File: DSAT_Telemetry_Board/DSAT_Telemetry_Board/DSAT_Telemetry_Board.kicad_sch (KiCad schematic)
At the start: 24 parts

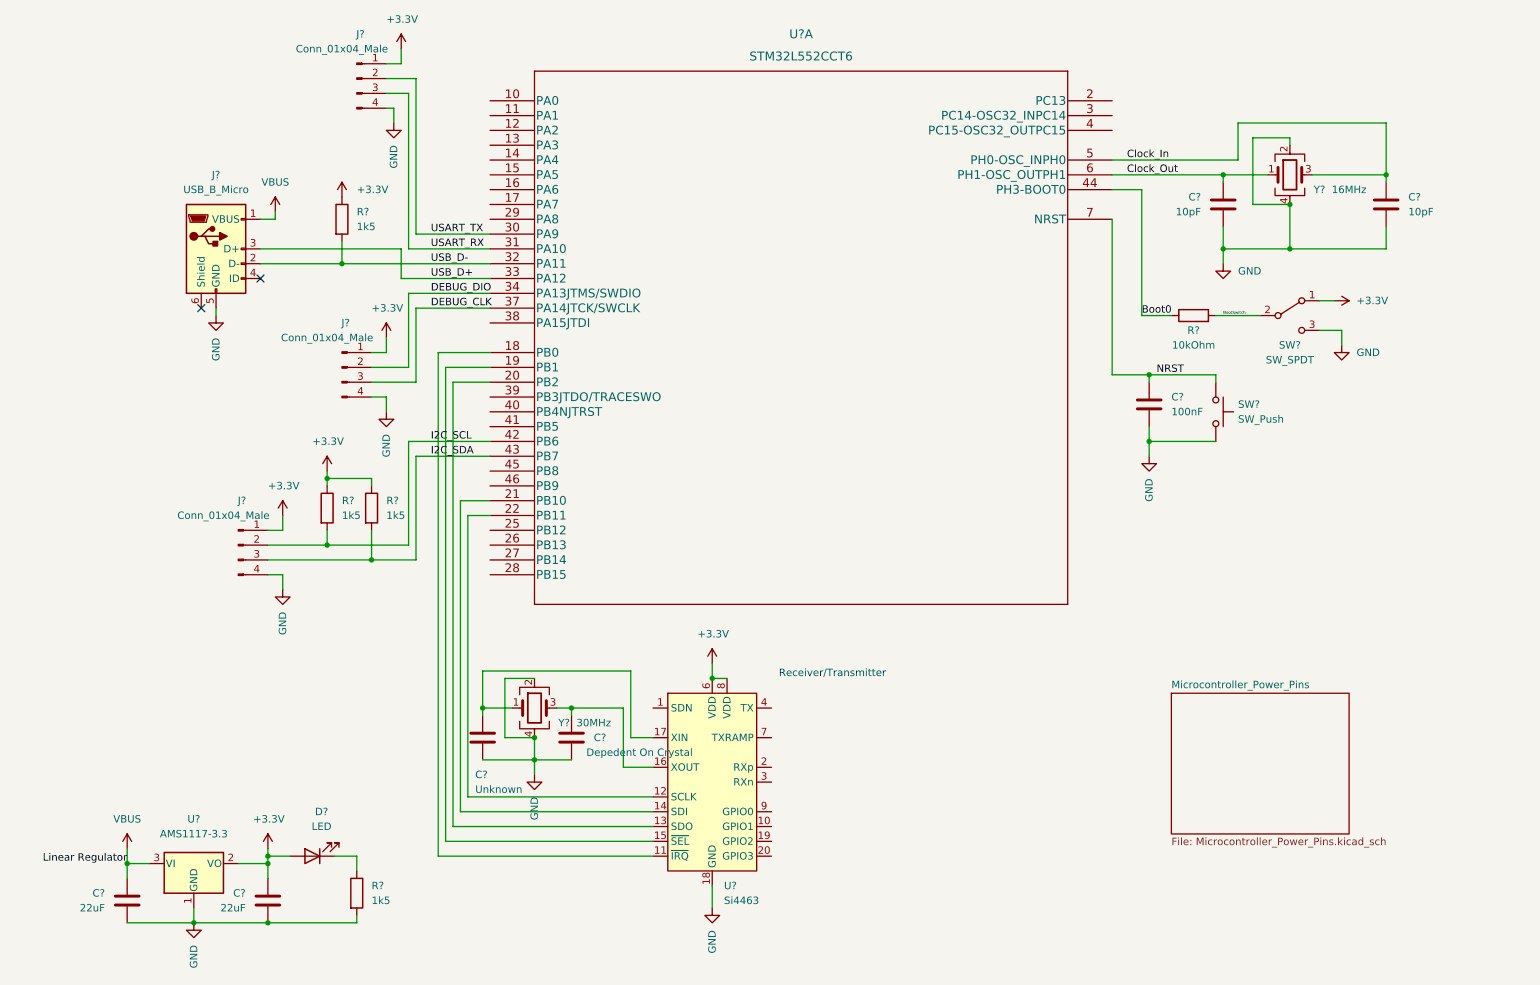
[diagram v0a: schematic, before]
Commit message: Added Hiarchical Sheets
Placed Modules into hiarchical sheets
Added Power supply section + Transcievers
Need to finish conncecting SI transciever chips and the bias tee on the chips + duplexer + LNA
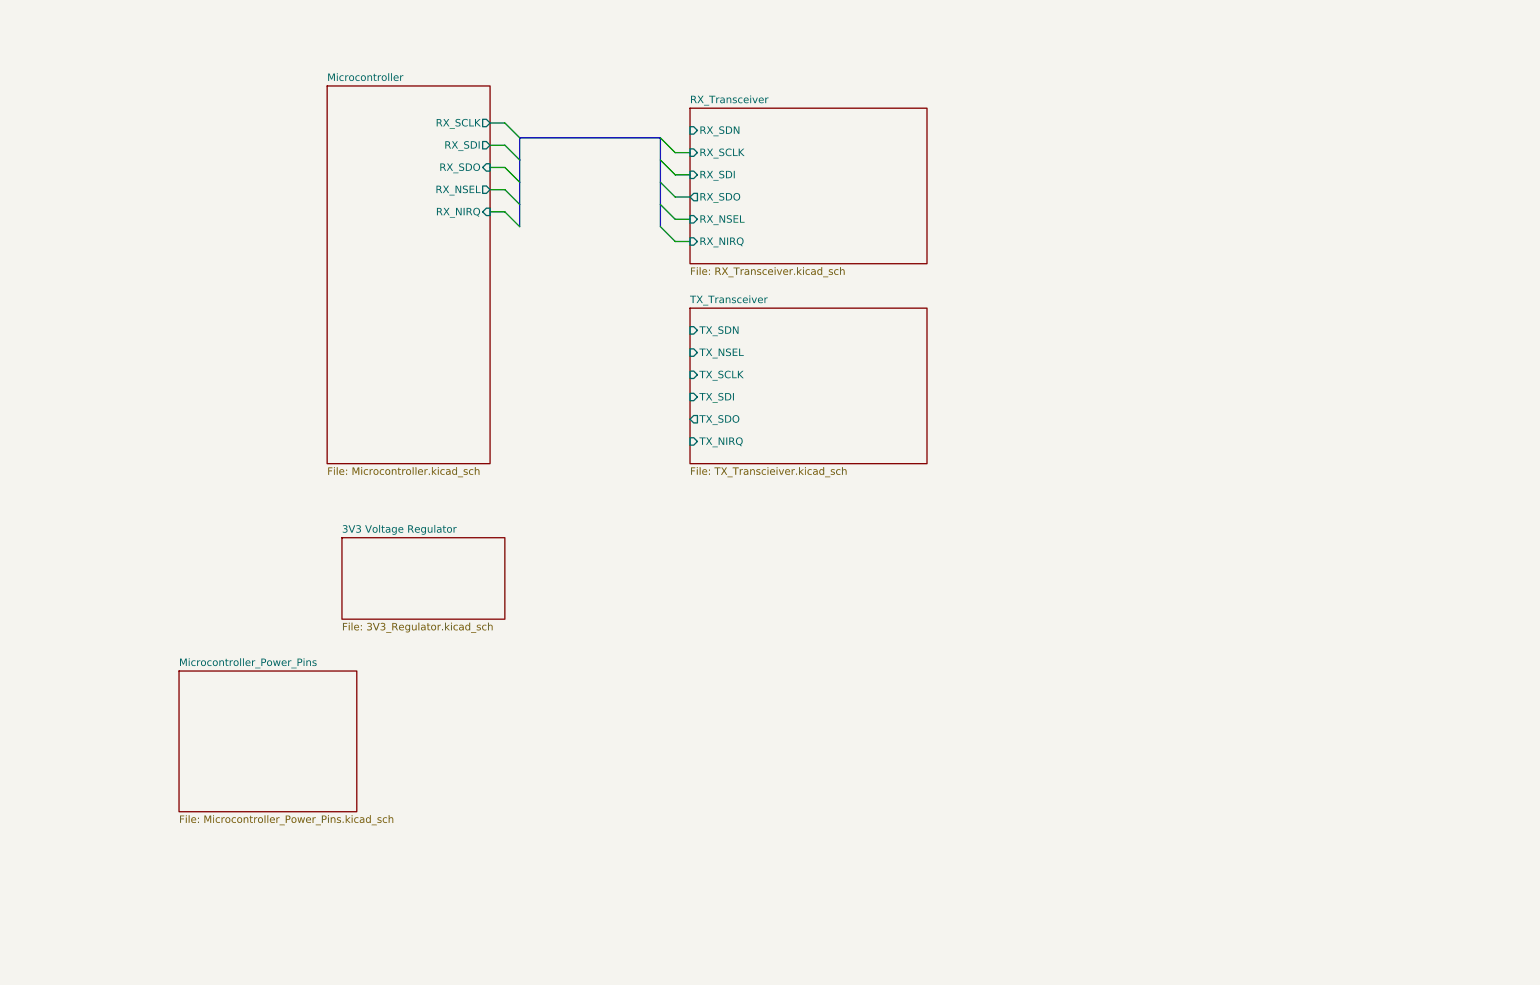
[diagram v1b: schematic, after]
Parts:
- removed C?: Unknown, symbol Device:C
- removed C? (x2): 22uF, symbol Device:C
- removed C?: Depedent On Crystal, symbol Device:C
- removed C?: 100nF, symbol Device:C
- removed C? (x2): 10pF, symbol Device:C
- removed D?: LED, symbol Device:LED
- removed J?: USB_B_Micro, symbol Connector:USB_B_Micro
- removed J? (x3): Conn_01x04_Male, symbol Connector:Conn_01x04_Male
- removed R? (x4): 1k5, symbol Device:R
- removed R?: 10kOhm, symbol Device:R
- removed SW?: SW_SPDT, symbol Switch:SW_SPDT
- removed SW?: SW_Push, symbol Switch:SW_Push
- removed U?: Si4463, Package_DFN_QFN:QFN-20-1EP_4x4mm_P0.5mm_EP2.6x2.6mm_ThermalVias, symbol RF:Si4463
- removed U?: AMS1117-3.3, Package_TO_SOT_SMD:SOT-223-3_TabPin2, symbol Regulator_Linear:AMS1117-3.3
- removed U?: STM32L552CCT6, LQFP-48, symbol STM32L5:STM32L552CCT6
- removed Y?: 16MHz, symbol Device:Crystal_GND24
- removed Y?: 30MHz, symbol Device:Crystal_GND24
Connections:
- no-connect marks 2 -> 0
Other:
- added sheet 3V3 Voltage Regulator (3V3_Regulator.kicad_sch)
- added sheet Microcontroller (Microcontroller.kicad_sch)
- added sheet RX_Transceiver (RX_Transceiver.kicad_sch)
- added sheet TX_Transceiver (TX_Transcieiver.kicad_sch)
- note removed: "Receiver/Transmitter"

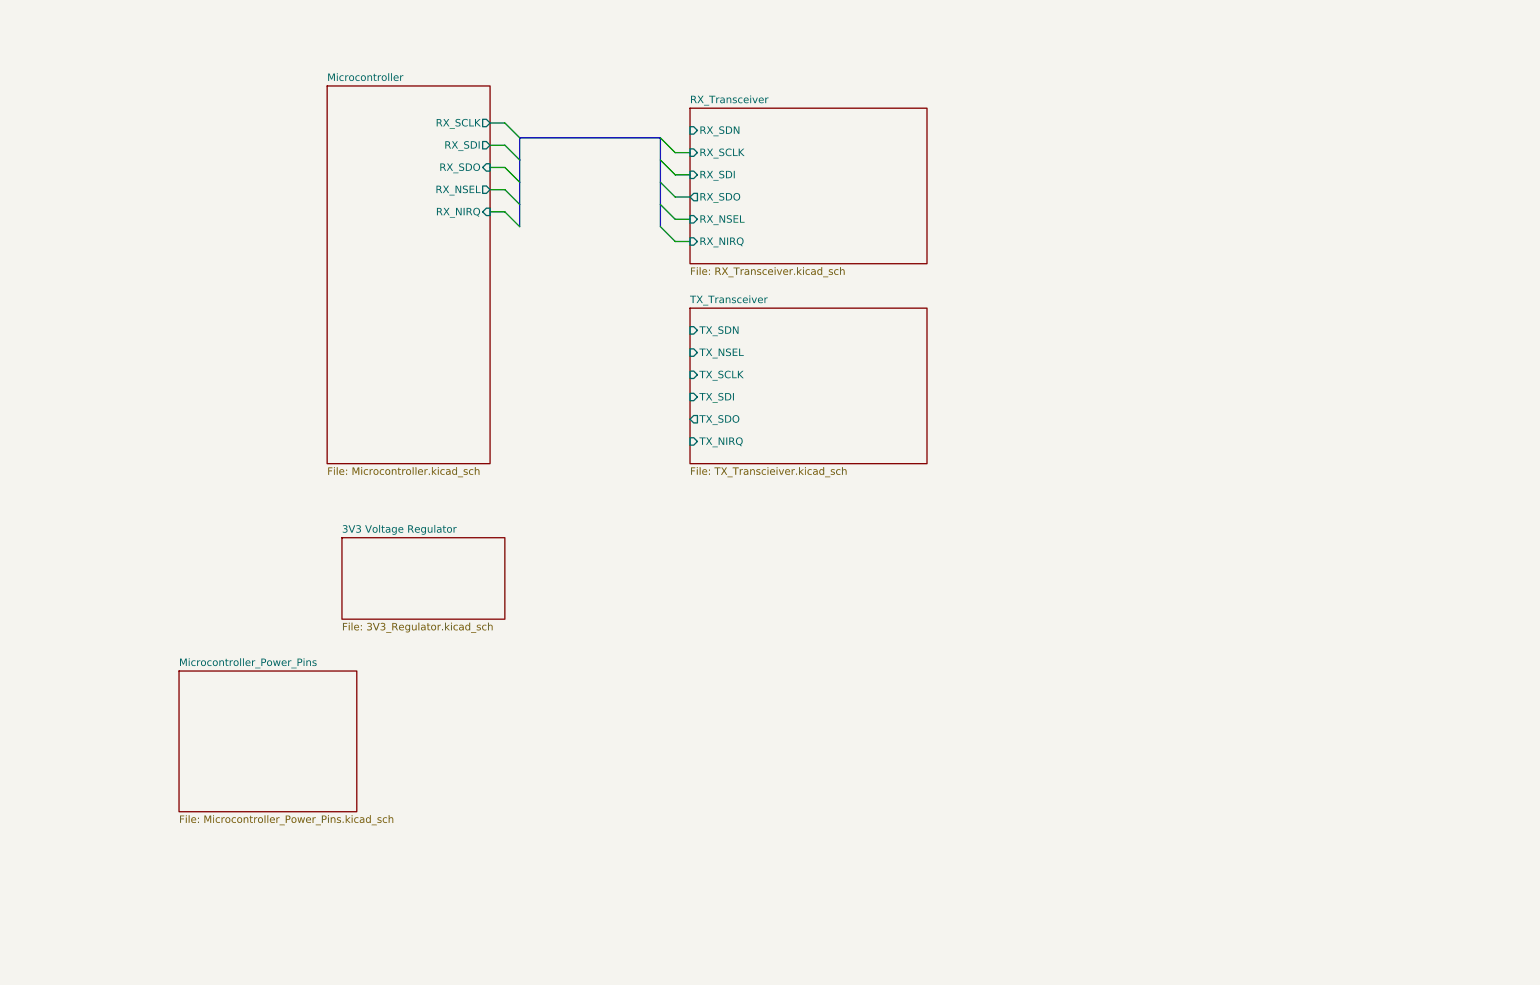
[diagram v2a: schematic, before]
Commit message: change to proper mcu and various schematic changes and additions
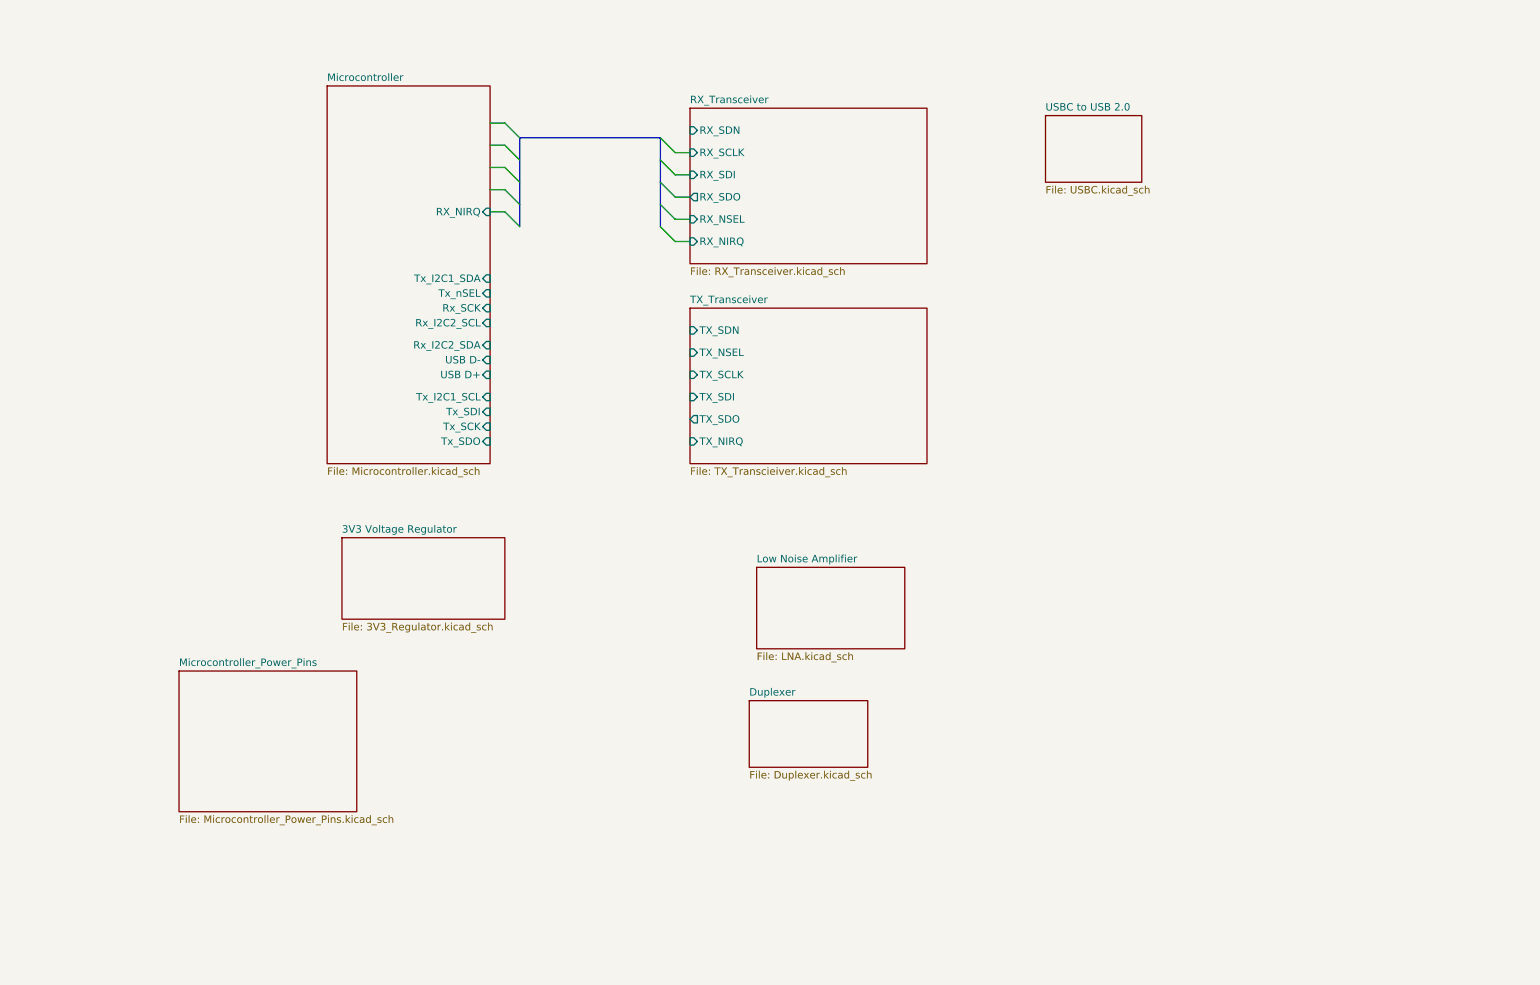
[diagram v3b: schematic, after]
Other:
- added sheet Duplexer (Duplexer.kicad_sch)
- added sheet Low Noise Amplifier (LNA.kicad_sch)
- added sheet USBC to USB 2.0 (USBC.kicad_sch)
- sheet Microcontroller ports: added Rx_I2C2_SCL, Rx_I2C2_SDA, Rx_SCK, Tx_I2C1_SCL, Tx_I2C1_SDA, Tx_SCK, Tx_SDI, Tx_SDO, Tx_nSEL, USB D+, USB D-; removed RX_NSEL, RX_SCLK, RX_SDI, RX_SDO
